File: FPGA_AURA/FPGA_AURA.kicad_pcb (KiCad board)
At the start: 6 copper layers, 50 x 50 mm, 147 parts, among them J1 TF-CARD_H1.8, J100 USB_C_Receptacle_USB2.0_16P, J101 XT30PW-M, J2 532617004, J3 532617007, J4 532617004, U1 XC7A35T-2FTG256C, U2 W25Q256JVEIQ, U200 ADP5014, U3 FT2232HQ, U4 TPS51200DRCR, U5 USBLC6-2SC6, U500 MT41K128M16JT-125_IT_K, U6 93LC56BT-I_SN, Y1 12MHz

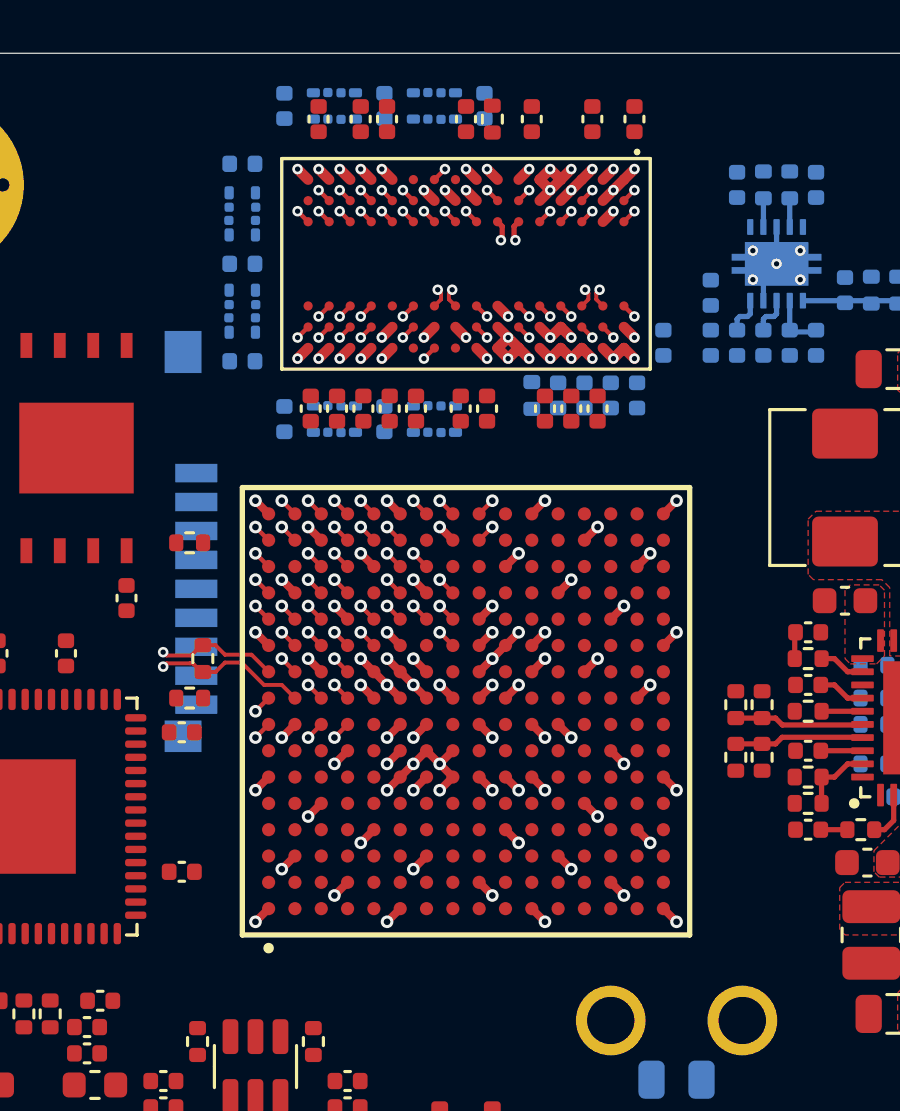
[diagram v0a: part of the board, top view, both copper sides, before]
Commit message: Moved to KiCAD V10 for delay.
The FPGA PCB has now been moved to KiCAD V10 to make use of the new delay features and design rules are being setup.

PCB stack-up has now been decided.
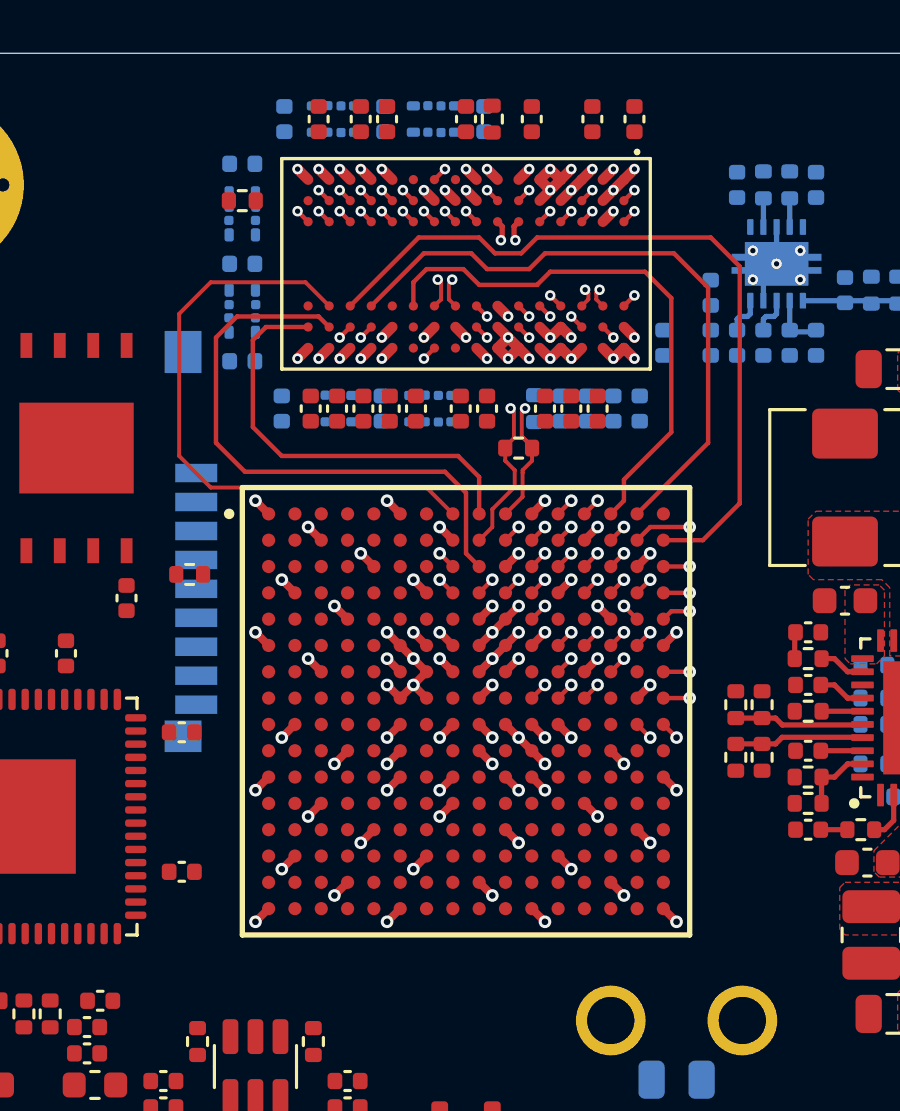
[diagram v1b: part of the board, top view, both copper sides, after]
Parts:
- moved R522 14.4 mm to (127.0, 65.0), turned to 0 degrees
- moved R524 13.2 mm to (116.5, 55.6)
- moved R1 4.70 mm to (114.5, 69.8)
- moved C515 0.51 mm to (129.6, 63.5)
- moved C518 0.51 mm to (131.6, 63.5)
- moved C520 0.51 mm to (128.6, 63.5)
- moved C524 0.51 mm to (130.6, 63.5)
- moved R523 0.51 mm to (127.6, 63.5)
- moved C502 0.50 mm to (118.1, 52.5)
- moved C503 0.50 mm to (121.9, 52.5)
- moved C505 0.50 mm to (125.7, 52.5)
- moved R509 0.50 mm to (123.8, 52.5)
- moved R513 0.50 mm to (120.0, 52.5)
- moved C506 0.41 mm to (121.8, 63.5)
- moved C500 0.41 mm to (118.0, 63.5)
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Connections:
- U1 pad A12: DDR3_A11 -> DDR3_BA1
- U1 pad A13: DDR3_A1 -> DDR3_BA2
- U1 pad A14: DDR3_A8 -> DDR3_A10
- U1 pad A15: DDR3_A6 -> DDR3_A12
- U1 pad A8: DDR3_BA2 -> DDR3_A11
- U1 pad A9: DDR3_WE -> DDR3_A8
- U1 pad B10: DDR3_A10 -> DDR3_A4
- U1 pad B11: DDR3_A12 -> DDR3_A0
- U1 pad B12: DDR3_A4 -> DDR3_A3
- U1 pad B14: unconnected-(U1D-IO_L8N_T1_AD10N_15-PadB14) -> DDR3_CAS
- U1 pad B15: DDR3_CAS -> DDR3_CS
- U1 pad B16: DDR3_BA1 -> DDR3_A1
- U1 pad C11: DDR3_A2 -> DDR3_CKE
- U1 pad C12: DDR3_A3 -> DDR3_BA0
- U1 pad C13: DDR3_ODT -> DDR3_A2
- U1 pad C16: DDR3_CKE -> DDR3_ODT
- U1 pad C8: DDR3_A0 -> DDR3_A7
- U1 pad C9: DDR3_A7 -> DDR3_A6
- U1 pad D10: DDR3_A5 -> DDR3_A13
- U1 pad D13: DDR3_BA0 -> DDR3_WE
- U1 pad D8: DDR3_A13 -> DDR3_A5
- U1 pad E13: unconnected-(U1D-IO_L13N_T2_MRCC_15-PadE13) -> DDR3_DM1
- U1 pad G15: unconnected-(U1D-IO_L24N_T3_RS0_15-PadG15) -> DDR3_DM0
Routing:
- net DDR3_A7: track 61.2 -> 26.4 mm
- net DDR3_CS: track 0.57 -> 30.8 mm, vias 1 -> 2
- net DDR3_A2: track 57.0 -> 26.8 mm
- net DDR3_A3: track 51.1 -> 21.0 mm
- net DDR3_A5: track 60.2 -> 30.5 mm
- net DDR3_A9: track 52.8 -> 23.9 mm
- net DDR3_DQS0+: track 1.50 -> 24.4 mm
- net DDR3_DQS0-: track 1.50 -> 23.1 mm
- net DDR3_BA0: track 44.4 -> 23.7 mm
- net DDR3_DQS1+: track 1.48 -> 20.5 mm
- net DDR3_DQS1-: track 1.48 -> 19.7 mm
- net DDR3_A13: track 44.6 -> 26.8 mm
- net DDR3_A0: track 40.9 -> 23.3 mm
- net DDR3_BA2: track 36.5 -> 19.4 mm
- net DDR3_A1: track 15.9 -> 29.3 mm, vias 2 -> 0
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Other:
- copper layers 6 -> 8

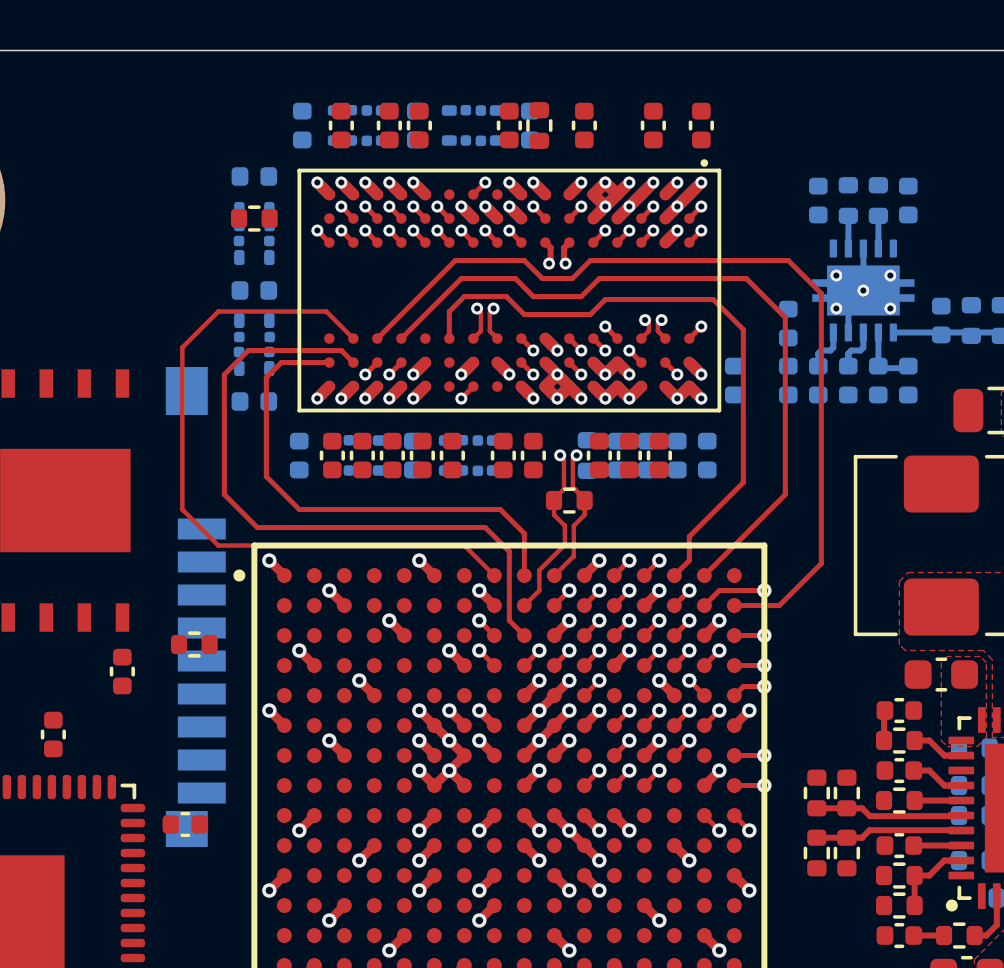
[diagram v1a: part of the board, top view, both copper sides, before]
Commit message: Time domain tuning setup.
The tuning profiles and net classes have been setup to enable time domain tuning.
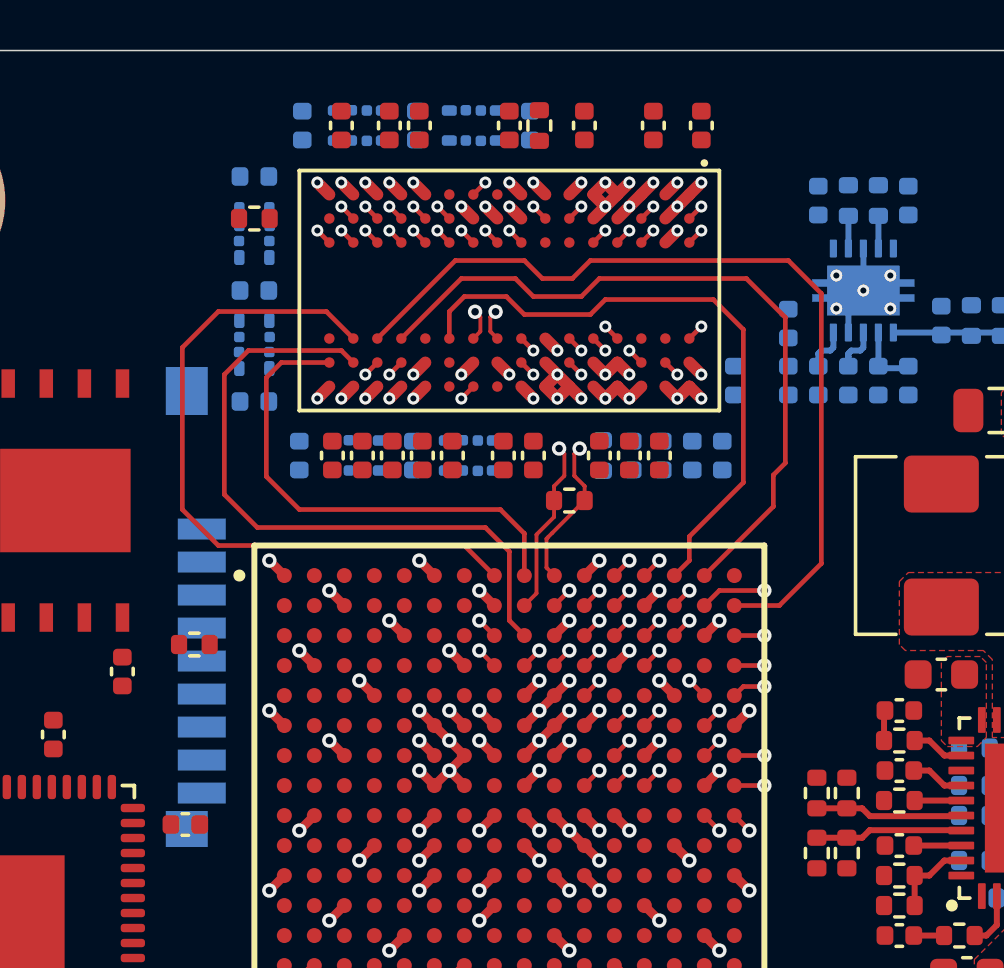
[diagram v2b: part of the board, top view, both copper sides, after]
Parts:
- moved C515 0.50 mm to (130.1, 63.5)
- moved C518 0.50 mm to (132.1, 63.5)
- moved C520 0.50 mm to (129.1, 63.5)
- moved C524 0.50 mm to (131.1, 63.5)
- moved R523 0.50 mm to (128.1, 63.5)
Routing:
- net DDR3_DQ4: track 1.27 -> 28.1 mm
- net DDR3_DQS0+: track 24.4 -> 0.00 mm, vias 2 -> 0
- net DDR3_DQS0-: track 23.1 -> 0.00 mm, vias 2 -> 0
- net DDR3_DQ5: track 1.27 -> 23.1 mm
- net DDR3_DQS1+: track 20.5 -> 0.00 mm, vias 2 -> 0
- net DDR3_DQ2: track 1.27 -> 21.3 mm
- net DDR3_DQS1-: track 19.7 -> 0.00 mm, vias 2 -> 0
- net DDR3_DQ0: track 1.27 -> 16.0 mm
- net DDR3_DQ13: track 10.2 -> 1.27 mm
- net DDR3_DQ11: track 8.89 -> 1.27 mm
- net DDR3_DQ8: track 7.48 -> 1.27 mm
- net DDR3_CK-: track 26.8 -> 25.5 mm
- net DDR3_CK+: track 26.5 -> 25.3 mm
- net DDR3_A3: track 21.0 -> 21.7 mm
- net DDR3_DM0: track 0.57 -> 1.27 mm, vias 1 -> 2
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
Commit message: Recovery after being partially deleted.
Revert to prior than this if this version is broken due to OneDrive sync issue.
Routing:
- net DDR3_DQ7: track 1.57 -> 28.2 mm
- net DDR3_DM0: track 1.27 -> 25.8 mm
- net DDR3_DQ3: track 1.57 -> 25.1 mm
- net DDR3_DQS0+: track 0.00 -> 22.9 mm, vias 0 -> 1
- net DDR3_DQS0-: track 0.00 -> 21.1 mm, vias 0 -> 1
- net DDR3_DQ2: track 21.3 -> 1.27 mm
- net DDR3_DQ0: track 16.0 -> 1.27 mm
- net DDR3_DQ5: track 23.1 -> 31.7 mm
- net DDR3_ODT: track 31.7 -> 37.4 mm
- net DDR3_DQS1+: track 0.00 -> 5.51 mm, vias 0 -> 1
- net DDR3_DQS1-: track 0.00 -> 5.51 mm, vias 0 -> 1
- net DDR3_CS: track 30.8 -> 36.0 mm
- net DDR3_DQ4: track 28.1 -> 30.6 mm
- net GND: track 50.8 -> 51.8 mm
- net DDR3_DQ13: track 1.27 -> 2.27 mm

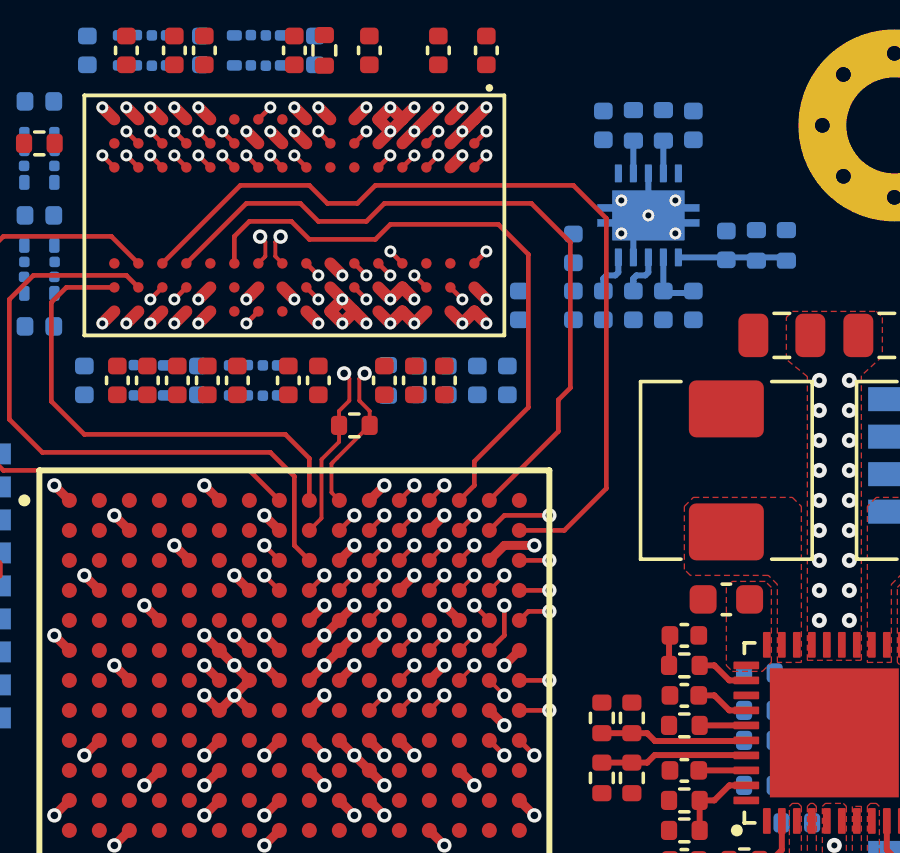
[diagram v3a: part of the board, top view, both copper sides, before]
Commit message: Fixed delay matching issue and started data lines
The delay matching is now working again and the data byte lanes are in the process of being routed.
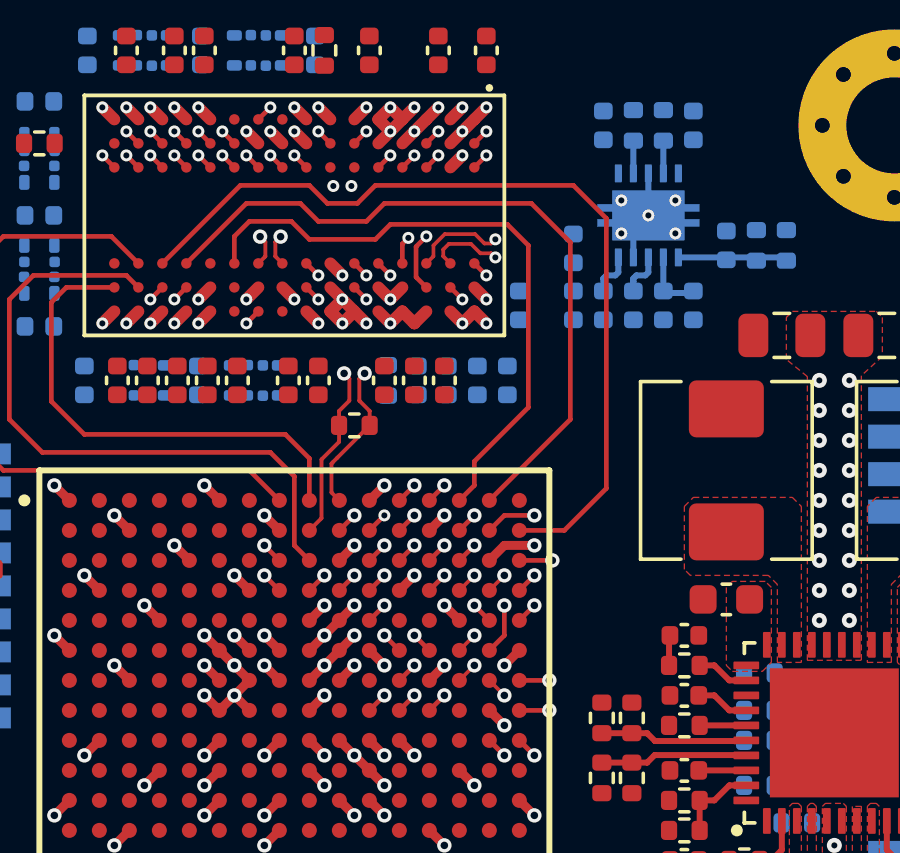
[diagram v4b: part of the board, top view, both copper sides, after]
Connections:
- U1 pad D11: DDR3_DQ10 -> DDR3_DQ1
- U1 pad D14: DDR3_DQS1+ -> DDR3_DQS0+
- U1 pad D15: DDR3_DQS1- -> DDR3_DQS0-
- U1 pad D16: DDR3_DQ9 -> DDR3_DQ3
- U1 pad E11: DDR3_DQ14 -> DDR3_DQ0
- U1 pad E13: DDR3_DM1 -> DDR3_DM0
- U1 pad E15: DDR3_DQ8 -> DDR3_DQ5
- U1 pad E16: DDR3_DQ15 -> DDR3_DQ7
- U1 pad F12: DDR3_DQ12 -> DDR3_DQ2
- U1 pad F13: DDR3_DQ11 -> DDR3_DQ6
- U1 pad F14: DDR3_DQS0- -> DDR3_DQS1-
- U1 pad F15: DDR3_DQ13 -> DDR3_DQ4
- U1 pad G12: DDR3_DQ1 -> DDR3_DQ10
- U1 pad G14: DDR3_DQS0+ -> DDR3_DQS1+
- U1 pad G15: DDR3_DM0 -> DDR3_DQ9
- U1 pad G16: DDR3_DQ3 -> DDR3_DQ14
- U1 pad H11: DDR3_DQ0 -> DDR3_DM1
- U1 pad H12: DDR3_DQ2 -> DDR3_DQ11
- U1 pad H13: DDR3_DQ6 -> DDR3_DQ8
- U1 pad H16: DDR3_DQ7 -> DDR3_DQ15
- U1 pad J15: DDR3_DQ4 -> DDR3_DQ13
- U1 pad J16: DDR3_DQ5 -> DDR3_DQ12
- U500 pad A7: DDR3_DQ12 -> DDR3_DQ8
- U500 pad C2: DDR3_DQ11 -> DDR3_DQ12
- U500 pad D7: DDR3_DQ8 -> DDR3_DQ11
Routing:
- net DDR3_DQ12: track 1.27 -> 32.3 mm
- net DDR3_DQ5: track 31.7 -> 1.27 mm
- net DDR3_DM1: track 0.57 -> 29.1 mm, vias 1 -> 2
- net DDR3_DQ4: track 30.6 -> 2.27 mm
- net DDR3_DQ7: track 28.2 -> 1.27 mm
- net DDR3_DQ13: track 2.27 -> 29.0 mm
- net DDR3_DM0: track 25.8 -> 0.57 mm, vias 2 -> 1
- net DDR3_DQ9: track 1.57 -> 26.3 mm
- net DDR3_DQ8: track 1.27 -> 25.1 mm
- net DDR3_DQ3: track 25.1 -> 1.27 mm
- net DDR3_DQ14: track 1.27 -> 25.1 mm
- net DDR3_DQ15: track 1.69 -> 25.1 mm
- net DDR3_DQ10: track 1.27 -> 22.7 mm
- net DDR3_DQS1+: track 5.51 -> 22.5 mm, vias 1 -> 2
- net DDR3_DQS1-: track 5.51 -> 20.6 mm, vias 1 -> 2
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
